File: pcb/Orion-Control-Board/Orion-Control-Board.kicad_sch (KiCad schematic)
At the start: 59 parts, among them J1 CONN_20_POS_KEYED_SOCKET, U1 BNO055, U2 INA3221, U3 DFR0753 5V BUCK, U4 PCA9685_PWM_SERVO_DRIVER_IC, U5 INA3221, U6 INA3221, Y1 32.768 kHz

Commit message: Update symbols
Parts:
- U2, U5, U6: footprint Package_DFN_QFN:Texas_RGV0016A_VQFN-16-1EP_4x4mm_P0.65mm_EP2.1x2.1mm -> AA_Custom_Components:Texas_RGV0016A_VQFN-16-1EP_4x4mm_P0.65mm_EP2.1x2.1mm_ThermalVias
- U4: footprint Silicon-Standard:TSSOP-28_4MM -> AA_Custom_Components:TSSOP-28_4MM
- Y1: footprint Clocks:CRYSTAL-SMD-3.2X1.5MM -> CRYSTAL-SMD-3.2X1.5MM; JLCPCB Part # C32346 -> C97606
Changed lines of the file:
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@@
 			)
 		)
-		(property "Description" ""
+		(property "Description" "Power symbol creates a global label with name \"+3.3V\""
 			(at 218.44 109.22 0)
 			(effects
@@
 					(size 1.27 1.27)
 				)
+				(hide yes)
 			)
 		)
@@
 			)
 		)
-		(property "Description" ""
+		(property "Description" "Ground Supply (Earth Ground style) Ground supply with a traditional \"earth ground\" symbol."
 			(at 60.96 185.42 0)
 			(effects
@@
 					(size 1.27 1.27)
 				)
+				(hide yes)
 			)
 		)
@@
 			)
 		)
-		(property "Description" ""
+		(property "Description" "Power symbol creates a global label with name \"+3.3V\""
 			(at 203.2 36.83 0)
 			(effects
@@
 					(size 1.27 1.27)
 				)
+				(hide yes)
 			)
 		)
@@
 			)
 		)
-		(property "Footprint" "Package_DFN_QFN:Texas_RGV0016A_VQFN-16-1EP_4x4mm_P0.65mm_EP2.1x2.1mm"
+		(property "Footprint" "AA_Custom_Components:Texas_RGV0016A_VQFN-16-1EP_4x4mm_P0.65mm_EP2.1x2.1mm_ThermalVias"
 			(at 198.12 105.41 0)
 			(effects
@@
 			)
 		)
-		(property "Description" ""
+		(property "Description" "Power symbol creates a global label with name \"+3.3V\""
 			(at 228.6 36.83 0)
 			(effects
@@
 					(size 1.27 1.27)
 				)
+				(hide yes)
 			)
 		)
@@
 			)
 		)
-		(property "Description" ""
+		(property "Description" "Power symbol creates a global label with name \"+3.3V\""
 			(at 68.58 109.22 0)
 			(effects
@@
 					(size 1.27 1.27)
 				)
+				(hide yes)
 			)
 		)
@@
 			)
 		)
-		(property "Description" ""
+		(property "Description" "Power symbol creates a global label with name \"+3.3V\""
 			(at 62.23 38.1 0)
 			(effects
@@
 					(size 1.27 1.27)
 				)
+				(hide yes)
 			)
 		)
@@
 			)
 		)
-		(property "Description" ""
+		(property "Description" "Ground Supply (Earth Ground style) Ground supply with a traditional \"earth ground\" symbol."
 			(at 106.68 76.2 0)
 			(effects
@@
 					(size 1.27 1.27)
 				)
+				(hide yes)
 			)
 		)
@@
 			)
 		)
-		(property "Description" ""
+		(property "Description" "Power symbol creates a global label with name \"+3.3V\""
 			(at 21.59 142.24 0)
 			(effects
@@
 					(size 1.27 1.27)
 				)
+				(hide yes)
 			)
 		)
@@
 			)
 		)
-		(property "Datasheet" "https://jlcpcb.com/api/file/downloadByFileSystemAccessId/8579709195039801344"
+		(property "Datasheet" "~"
 			(at 247.65 73.66 0)
 			(effects
@@
 			)
 		)
+		(property "Sim.Pins" "1=K 2=A"
+			(at 247.65 73.66 0)
+			(effects
+				(font
+					(size 1.27 1.27)
+				)
+				(hide yes)
+			)
+		)
 		(pin "1"
 		)
@@
 			)
 		)
-		(property "Description" ""
+		(property "Description" "Power symbol creates a global label with name \"+5VD\""
 			(at 227.33 69.85 0)
 			(effects
@@
 			)
 		)
-		(property "Description" ""
+		(property "Description" "Ground Supply (Earth Ground style) Ground supply with a traditional \"earth ground\" symbol."
 			(at 147.32 55.88 0)
 			(effects
@@
 					(size 1.27 1.27)
 				)
+				(hide yes)
 			)
 		)
@@
 			)
 		)
-		(property "Footprint" "Clocks:CRYSTAL-SMD-3.2X1.5MM"
+		(property "Footprint" "CRYSTAL-SMD-3.2X1.5MM"
 			(at 69.85 59.69 0)
 			(effects
@@
 			)
 		)
-		(property "JLCPCB Part #" "C32346"
+		(property "JLCPCB Part #" "C97606"
 			(at 67.056 64.77 0)
 			(effects
@@
 			)
 		)
-		(property "Description" ""
+		(property "Description" "Power symbol creates a global label with name \"+3.3V\""
 			(at 21.59 46.99 0)
 			(effects
@@
 					(size 1.27 1.27)
 				)
+				(hide yes)
 			)
 		)
@@
 	)
 	(symbol
-		(lib_name "LED_5")
 		(lib_id "Device:LED")
 		(at 227.33 73.66 90)
@@
 			)
 		)
-		(property "Datasheet" "https://jlcpcb.com/api/file/downloadByFileSystemAccessId/8550723991833485312"
+		(property "Datasheet" "~"
 			(at 227.33 73.66 0)
 			(effects
@@
 			)
 		)
+		(property "Sim.Pins" "1=K 2=A"
+			(at 227.33 73.66 0)
+			(effects
+				(font
+					(size 1.27 1.27)
+				)
+				(hide yes)
+			)
+		)
 		(pin "1"
 		)
@@
 	)
 	(symbol
-		(lib_name "LED_5")
 		(lib_id "Device:LED")
 		(at 207.01 73.66 90)
@@
 			)
 		)
-		(property "Datasheet" "https://jlcpcb.com/api/file/downloadByFileSystemAccessId/8639582106239348736"
+		(property "Datasheet" "~"
 			(at 207.01 73.66 0)
 			(effects
@@
 			)
 		)
+		(property "Sim.Pins" "1=K 2=A"
+			(at 207.01 73.66 0)
+			(effects
+				(font
+					(size 1.27 1.27)
+				)
+				(hide yes)
+			)
+		)
 		(pin "1"
 		)
@@
 	)
 	(symbol
-		(lib_name "INA3221_2")
 		(lib_id "AA_Custom_Components:INA3221")
 		(at 124.46 134.62 0)
@@
 			)
 		)
-		(property "Footprint" "Package_DFN_QFN:Texas_RGV0016A_VQFN-16-1EP_4x4mm_P0.65mm_EP2.1x2.1mm"
+		(property "Footprint" "AA_Custom_Components:Texas_RGV0016A_VQFN-16-1EP_4x4mm_P0.65mm_EP2.1x2.1mm_ThermalVias"
 			(at 124.46 105.41 0)
 			(effects
@@
 	)
 	(symbol
-		(lib_name "INA3221_1")
 		(lib_id "AA_Custom_Components:INA3221")
 		(at 48.26 134.62 0)
@@
 			)
 		)
-		(property "Footprint" "Package_DFN_QFN:Texas_RGV0016A_VQFN-16-1EP_4x4mm_P0.65mm_EP2.1x2.1mm"
+		(property "Footprint" "AA_Custom_Components:Texas_RGV0016A_VQFN-16-1EP_4x4mm_P0.65mm_EP2.1x2.1mm_ThermalVias"
 			(at 48.26 105.41 0)
 			(effects
@@
 			)
 		)
-		(property "Footprint" "Silicon-Standard:TSSOP-28_4MM"
+		(property "Footprint" "AA_Custom_Components:TSSOP-28_4MM"
 			(at 120.65 36.83 0)
 			(effects
@@
 			)
 		)
-		(property "Description" ""
+		(property "Description" "Power symbol creates a global label with name \"+5VD\""
 			(at 207.01 69.85 0)
 			(effects
@@
 					(size 1.27 1.27)
 				)
+				(hide yes)
 			)
 		)
@@
 			)
 		)
-		(property "Description" ""
+		(property "Description" "Power symbol creates a global label with name \"+5VD\""
 			(at 74.93 171.45 0)
 			(effects
@@
 					(size 1.27 1.27)
 				)
+				(hide yes)
 			)
 		)
@@
 			)
 		)
-		(property "Description" ""
+		(property "Description" "Power symbol creates a global label with name \"+5VD\""
 			(at 186.69 69.85 0)
 			(effects
@@
 					(size 1.27 1.27)
 				)
+				(hide yes)
 			)
 		)
@@
 			)
 		)
-		(property "Description" ""
+		(property "Description" "Power symbol creates a global label with name \"+3.3V\""
 			(at 151.13 38.1 0)
 			(effects
@@
 					(size 1.27 1.27)
 				)
+				(hide yes)
 			)
 		)
@@
 			)
 		)
-		(property "Description" ""
+		(property "Description" "Power symbol creates a global label with name \"+3.3V\""
 			(at 144.78 109.22 0)
 			(effects
@@
 					(size 1.27 1.27)
 				)
+				(hide yes)
 			)
 		)
@@
 			)
 		)
-		(property "Description" ""
+		(property "Description" "Ground Supply (Earth Ground style) Ground supply with a traditional \"earth ground\" symbol."
 			(at 207.01 85.09 0)
 			(effects
@@
 					(size 1.27 1.27)
 				)
+				(hide yes)
 			)
 		)
@@
 			)
 		)
-		(property "Description" ""
+		(property "Description" "Ground Supply (Earth Ground style) Ground supply with a traditional \"earth ground\" symbol."
 			(at 91.44 48.26 0)
 			(effects
@@
 					(size 1.27 1.27)
 				)
+				(hide yes)
 			)
 		)
@@
 	)
 	(symbol
-		(lib_name "LED_5")
 		(lib_id "Device:LED")
 		(at 186.69 73.66 90)
@@
 			)
 		)
-		(property "Datasheet" "https://jlcpcb.com/api/file/downloadByFileSystemAccessId/8639582106239348736"
+		(property "Datasheet" "~"
 			(at 186.69 73.66 0)
 			(effects
@@
 			)
 		)
+		(property "Sim.Pins" "1=K 2=A"
+			(at 186.69 73.66 0)
+			(effects
+				(font
+					(size 1.27 1.27)
+				)
+				(hide yes)
+			)
+		)
 		(pin "1"
 		)
@@
 			)
 		)
-		(property "Description" ""
-			(at 186.69 85.09 0)
+		(property "Description" "Ground Supply (Earth Ground style) Ground supply with a traditional \"earth ground\" symbol."
+			(at 203.962 95.758 0)
 			(effects
 				(font
 					(size 1.27 1.27)
 				)
+				(hide yes)
 			)
 		)

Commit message: Route IMU and Servo Driver
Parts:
- JP1, JP2, JP3, JP4, JP7: footprint AA_Custom_Components:Jumper_PinHeader_1x02_P2.54mm_Vertical -> AA_Custom_Components:Jumper_PinHeader_1x02_P2.54mm_Vertical_Bridged
- Y1: footprint CRYSTAL-SMD-3.2X1.5MM -> AA_Custom_Components:CRYSTAL-SMD-3.2X1.5MM
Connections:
- net +3.3V: no longer U1.11 (~{RESET}), U1.4 (~{BOOT_LOAD_PIN})
- net 2S_BATT_FRONT_CELL1: now also J1.16; no longer J1.18
- net 2S_BATT_FRONT_CELL2: now also J1.14; no longer J1.20
- net 2S_BATT_REAR_CELL1: now also J1.20; no longer J1.14
- net 2S_BATT_REAR_CELL2: now also J1.18; no longer J1.16
- net 3S_BATT_CELL1: now also J1.17; no longer J1.13
- net 3S_BATT_CELL3: now also J1.13; no longer J1.17
- net 3V3_BNO: now reaches C1.2, C2.1, JP1.1 (A), U1.28 (VDDIO), U1.3 (VDD)
- net 3V3_BNO: now also U1.11 (~{RESET}), U1.4 (~{BOOT_LOAD_PIN})
- net Y-: now reaches C6.2, U1.27 (XIN32), Y1.P$2 (2)
- net Y+: now reaches C5.1, U1.26 (XOUT32), Y1.P$1 (1)
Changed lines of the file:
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@@
 	)
 	(junction
-		(at 21.59 53.34)
-		(diameter 0)
-		(color 0 0 0 0)
-	)
-	(junction
 		(at 173.99 129.54)
 		(diameter 0)
@@
 	(wire
 		(pts
-			(xy 21.59 46.99) (xy 21.59 53.34)
-		)
-		(stroke
-			(width 0)
-			(type default)
-		)
-	)
-	(wire
-		(pts
 			(xy 128.27 115.57) (xy 138.43 115.57)
 		)
@@
 		)
 	)
+	(label "3V3_BNO"
+		(at 46.99 38.1 180)
+		(effects
+			(font
+				(size 1.27 1.27)
+			)
+			(justify right bottom)
+		)
+	)
+	(label "Y+"
+		(at 62.23 53.34 0)
+		(effects
+			(font
+				(size 1.27 1.27)
+			)
+			(justify left bottom)
+		)
+	)
+	(label "3V3_BNO"
+		(at 21.59 53.34 0)
+		(effects
+			(font
+				(size 1.27 1.27)
+			)
+			(justify left bottom)
+		)
+	)
+	(label "Y-"
+		(at 64.77 66.04 180)
+		(effects
+			(font
+				(size 1.27 1.27)
+			)
+			(justify right bottom)
+		)
+	)
 	(global_label "PWM0"
 		(shape output)
@@
 	(global_label "3S_BATT_CELL3"
 		(shape output)
-		(at 101.6 194.31 180)
+		(at 101.6 189.23 180)
 		(fields_autoplaced yes)
 		(effects
@@
 		)
 		(property "Intersheetrefs" "${INTERSHEET_REFS}"
-			(at 84.9363 194.31 0)
+			(at 84.9363 189.23 0)
 			(effects
 				(font
@@
 	(global_label "2S_BATT_FRONT_CELL2"
 		(shape output)
-		(at 118.11 196.85 0)
+		(at 118.11 189.23 0)
 		(fields_autoplaced yes)
 		(effects
@@
 		)
 		(property "Intersheetrefs" "${INTERSHEET_REFS}"
-			(at 141.7285 196.85 0)
+			(at 141.7285 189.23 0)
 			(effects
 				(font
@@
 	(global_label "2S_BATT_REAR_CELL2"
 		(shape output)
-		(at 118.11 191.77 0)
+		(at 118.11 194.31 0)
 		(fields_autoplaced yes)
 		(effects
@@
 		)
 		(property "Intersheetrefs" "${INTERSHEET_REFS}"
-			(at 140.5189 191.77 0)
+			(at 140.5189 194.31 0)
 			(effects
 				(font
@@
 	(global_label "3S_BATT_CELL1"
 		(shape output)
-		(at 101.6 189.23 180)
+		(at 101.6 194.31 180)
 		(fields_autoplaced yes)
 		(effects
@@
 		)
 		(property "Intersheetrefs" "${INTERSHEET_REFS}"
-			(at 84.9363 189.23 0)
+			(at 84.9363 194.31 0)
 			(effects
 				(font
@@
 	(global_label "2S_BATT_REAR_CELL1"
 		(shape output)
-		(at 118.11 189.23 0)
+		(at 118.11 196.85 0)
 		(fields_autoplaced yes)
 		(effects
@@
 		)
 		(property "Intersheetrefs" "${INTERSHEET_REFS}"
-			(at 140.5189 189.23 0)
+			(at 140.5189 196.85 0)
 			(effects
 				(font
@@
 	(global_label "2S_BATT_FRONT_CELL1"
 		(shape output)
-		(at 118.11 194.31 0)
+		(at 118.11 191.77 0)
 		(fields_autoplaced yes)
 		(effects
@@
 		)
 		(property "Intersheetrefs" "${INTERSHEET_REFS}"
-			(at 141.7285 194.31 0)
+			(at 141.7285 191.77 0)
 			(effects
 				(font
@@
 			)
 		)
-		(property "Footprint" "AA_Custom_Components:Jumper_PinHeader_1x02_P2.54mm_Vertical"
+		(property "Footprint" "AA_Custom_Components:Jumper_PinHeader_1x02_P2.54mm_Vertical_Bridged"
 			(at 53.34 38.1 0)
 			(effects
@@
 		(dnp no)
 		(property "Reference" "C1"
-			(at 38.2016 40.259 90)
+			(at 43.434 41.91 90)
 			(effects
 				(font
@@
 		)
 		(property "Value" "100nF"
-			(at 40.894 37.846 90)
+			(at 38.354 41.91 90)
 			(effects
 				(font
@@
 			)
 		)
-		(property "Footprint" "AA_Custom_Components:Jumper_PinHeader_1x02_P2.54mm_Vertical"
+		(property "Footprint" "AA_Custom_Components:Jumper_PinHeader_1x02_P2.54mm_Vertical_Bridged"
 			(at 57.15 110.49 0)
 			(effects
@@
 			)
 		)
-		(property "Footprint" "CRYSTAL-SMD-3.2X1.5MM"
+		(property "Footprint" "AA_Custom_Components:CRYSTAL-SMD-3.2X1.5MM"
 			(at 69.85 59.69 0)
 			(effects
@@
 	)
 	(symbol
-		(lib_id "power:+3.3V")
-		(at 21.59 46.99 0)
-		(unit 1)
-		(exclude_from_sim no)
-		(in_bom yes)
-		(on_board yes)
-		(dnp no)
-		(property "Reference" "#PWR01"
-			(at 21.59 50.8 0)
-			(effects
-				(font
-					(size 1.27 1.27)
-				)
-				(hide yes)
-			)
-		)
-		(property "Value" "+3.3V"
-			(at 21.971 42.5958 0)
-			(effects
-				(font
-					(size 1.27 1.27)
-				)
-			)
-		)
-		(property "Footprint" ""
-			(at 21.59 46.99 0)
-			(effects
-				(font
-					(size 1.27 1.27)
-				)
-				(hide yes)
-			)
-		)
-		(property "Datasheet" ""
-			(at 21.59 46.99 0)
-			(effects
-				(font
-					(size 1.27 1.27)
-				)
-				(hide yes)
-			)
-		)
-		(property "Description" "Power symbol creates a global label with name \"+3.3V\""
-			(at 21.59 46.99 0)
-			(effects
-				(font
-					(size 1.27 1.27)
-				)
-				(hide yes)
-			)
-		)
-		(pin "1"
-		)
-		(instances
-			(project "Orion-Control-Board"
-				(path "/0755aee5-bc01-4cb5-b830-583289df50a3"
-					(reference "#PWR01")
-					(unit 1)
-				)
-			)
-		)
-	)
-	(symbol
 		(lib_id "Device:R")
 		(at 31.75 124.46 270)
@@
 			)
 		)
-		(property "Footprint" "AA_Custom_Components:Jumper_PinHeader_1x02_P2.54mm_Vertical"
+		(property "Footprint" "AA_Custom_Components:Jumper_PinHeader_1x02_P2.54mm_Vertical_Bridged"
 			(at 133.35 110.49 0)
 			(effects
@@
 			)
 		)
-		(property "Footprint" "AA_Custom_Components:Jumper_PinHeader_1x02_P2.54mm_Vertical"
+		(property "Footprint" "AA_Custom_Components:Jumper_PinHeader_1x02_P2.54mm_Vertical_Bridged"
 			(at 142.24 38.1 0)
 			(effects
@@
 			)
 		)
-		(property "Footprint" "AA_Custom_Components:Jumper_PinHeader_1x02_P2.54mm_Vertical"
+		(property "Footprint" "AA_Custom_Components:Jumper_PinHeader_1x02_P2.54mm_Vertical_Bridged"
 			(at 207.01 110.49 0)
 			(effects

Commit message: Route more
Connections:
- net SCL_{2} is gone; now on net SCL_{3}: U2.6 (SCL), U5.6 (SCL), U6.5 (A0), U6.6 (SCL)
- net SDA_{2} is gone; now on net SDA_{3}: U2.7 (SDA), U5.5 (A0), U5.7 (SDA), U6.7 (SDA)
- net +3.3V: no longer U2.5 (A0)
- net at C4.1, JP2.1 (A), R1.2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: now also U2.5 (A0)
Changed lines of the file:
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@@
 	)
 	(junction
+		(at 24.13 132.08)
+		(diameter 0)
+		(color 0 0 0 0)
+	)
+	(junction
 		(at 100.33 129.54)
 		(diameter 0)
@@
 	(wire
 		(pts
+			(xy 24.13 142.24) (xy 36.83 142.24)
+		)
+		(stroke
+			(width 0)
+			(type default)
+		)
+	)
+	(wire
+		(pts
 			(xy 185.42 139.7) (xy 186.69 139.7)
 		)
@@
 	(wire
 		(pts
+			(xy 24.13 142.24) (xy 24.13 132.08)
+		)
+		(stroke
+			(width 0)
+			(type default)
+		)
+	)
+	(wire
+		(pts
 			(xy 224.79 39.37) (xy 228.6 39.37)
 		)
@@
 	(wire
 		(pts
-			(xy 21.59 142.24) (xy 36.83 142.24)
-		)
-		(stroke
-			(width 0)
-			(type default)
-		)
-	)
-	(wire
-		(pts
 			(xy 45.72 86.36) (xy 46.99 86.36)
 		)
@@
 		)
 	)
-	(global_label "SCL_{2}"
+	(global_label "SCL_{3}"
 		(shape bidirectional)
 		(at 110.49 139.7 180)
@@
 		)
 	)
-	(global_label "SDA_{2}"
+	(global_label "SDA_{3}"
 		(shape bidirectional)
 		(at 110.49 137.16 180)
@@
 		)
 	)
-	(global_label "SCL_{2}"
+	(global_label "SCL_{3}"
 		(shape bidirectional)
 		(at 184.15 139.7 180)
@@
 		)
 	)
-	(global_label "SDA_{2}"
+	(global_label "SDA_{3}"
 		(shape bidirectional)
 		(at 34.29 137.16 180)
@@
 		)
 	)
-	(global_label "SDA_{2}"
+	(global_label "SDA_{3}"
 		(shape bidirectional)
 		(at 184.15 137.16 180)
@@
 		)
 	)
-	(global_label "SCL_{2}"
+	(global_label "SCL_{3}"
 		(shape bidirectional)
 		(at 34.29 139.7 180)
@@
 					(unit 1)
 				)
-			)
-		)
-	)
-	(symbol
-		(lib_id "power:+3.3V")
-		(at 21.59 142.24 0)
-		(unit 1)
-		(exclude_from_sim no)
-		(in_bom yes)
-		(on_board yes)
-		(dnp no)
-		(property "Reference" "#PWR02"
-			(at 21.59 146.05 0)
-			(effects
-				(font
-					(size 1.27 1.27)
-				)
-				(hide yes)
-			)
-		)
-		(property "Value" "+3.3V"
-			(at 21.971 137.8458 0)
-			(effects
-				(font
-					(size 1.27 1.27)
-				)
-			)
-		)
-		(property "Footprint" ""
-			(at 21.59 142.24 0)
-			(effects
-				(font
-					(size 1.27 1.27)
-				)
-				(hide yes)
-			)
-		)
-		(property "Datasheet" ""
-			(at 21.59 142.24 0)
-			(effects
-				(font
-					(size 1.27 1.27)
-				)
-				(hide yes)
-			)
-		)
-		(property "Description" "Power symbol creates a global label with name \"+3.3V\""
-			(at 21.59 142.24 0)
-			(effects
-				(font
-					(size 1.27 1.27)
-				)
-				(hide yes)
-			)
-		)
-		(pin "1"
-		)
-		(instances
-			(project "Orion-Control-Board"
-				(path "/0755aee5-bc01-4cb5-b830-583289df50a3"
-					(reference "#PWR02")
-					(unit 1)
-				)

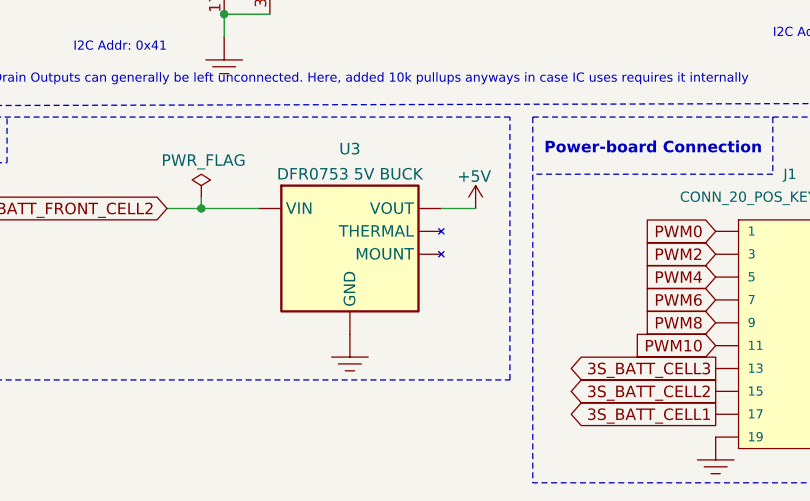
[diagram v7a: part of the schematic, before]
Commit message: Route all except voltage sensor
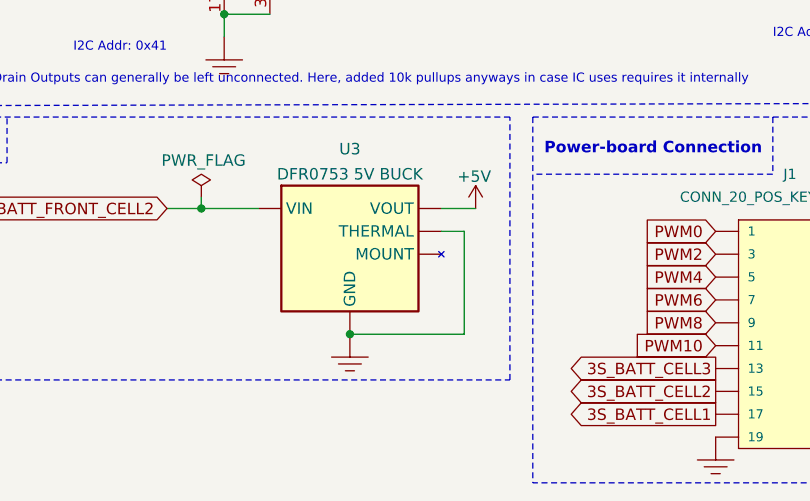
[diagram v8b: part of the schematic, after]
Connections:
- net GND: now also U3.4 (THERMAL)
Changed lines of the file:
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@@
+	)
+	(junction
+		(at 60.96 185.42)
+		(diameter 0)
+		(color 0 0 0 0)
 	)
 	(junction
@@
 	(wire
 		(pts
+			(xy 73.66 173.99) (xy 73.66 185.42)
+		)
+		(stroke
+			(width 0)
+			(type default)
+		)
+	)
+	(wire
+		(pts
 			(xy 128.27 116.84) (xy 128.27 115.57)
 		)
@@
 	(wire
 		(pts
+			(xy 73.66 185.42) (xy 60.96 185.42)
+		)
+		(stroke
+			(width 0)
+			(type default)
+		)
+	)
+	(wire
+		(pts
 			(xy 24.13 129.54) (xy 24.13 132.08)
 		)
@@
 		)
 		(stroke
+			(width 0)
+			(type default)
+		)
+	)
+	(wire
+		(pts
+			(xy 71.12 173.99) (xy 73.66 173.99)
+		)
+		(stroke
